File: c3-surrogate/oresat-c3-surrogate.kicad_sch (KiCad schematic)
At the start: 70 parts, among them J1 J-SAMTEC-TFM-120-X1-XXX-D-RA, J2 Conn_01x04, J4 Conn_01x02_Socket, Q1 PMV45EN, Q3 NTR2101P, Q4 NTR2101P, Q5 DMP3050LVT-7, SW2 Slide Switch, SW3 OS203011MV9QS1, SW4 EG1218, U1 MAX892LEUA+T, U2 LTC4412xS6, U4 LTC4412xS6, U5 TS5A21366, U6 Trinket-M0

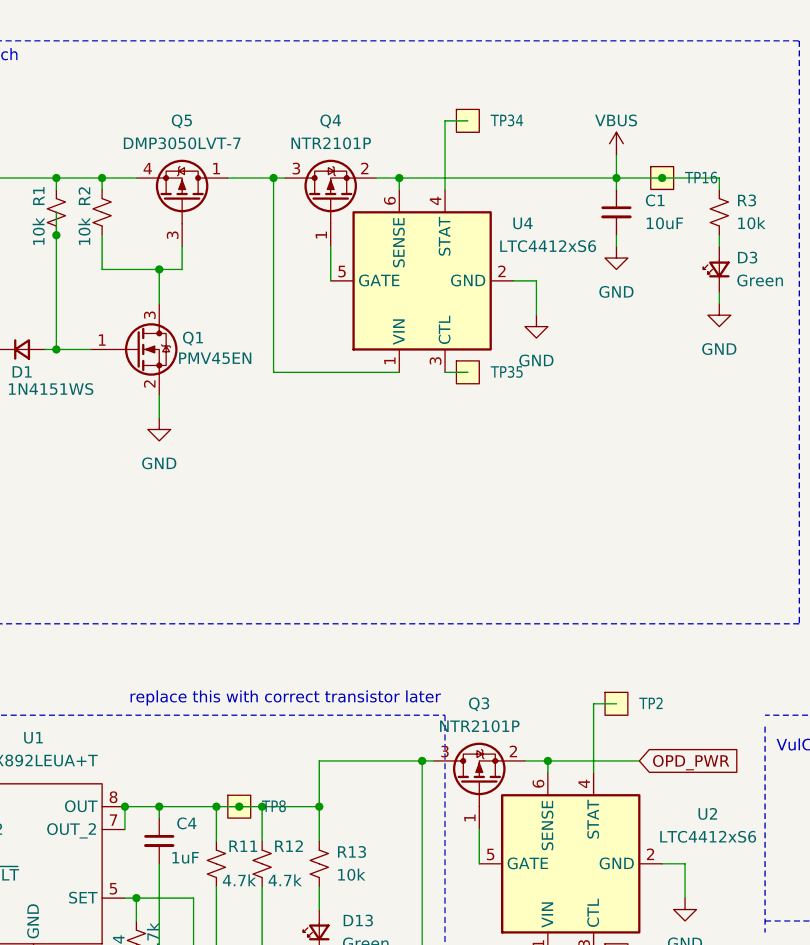
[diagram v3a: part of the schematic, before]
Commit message: modified pcb using updated schematic
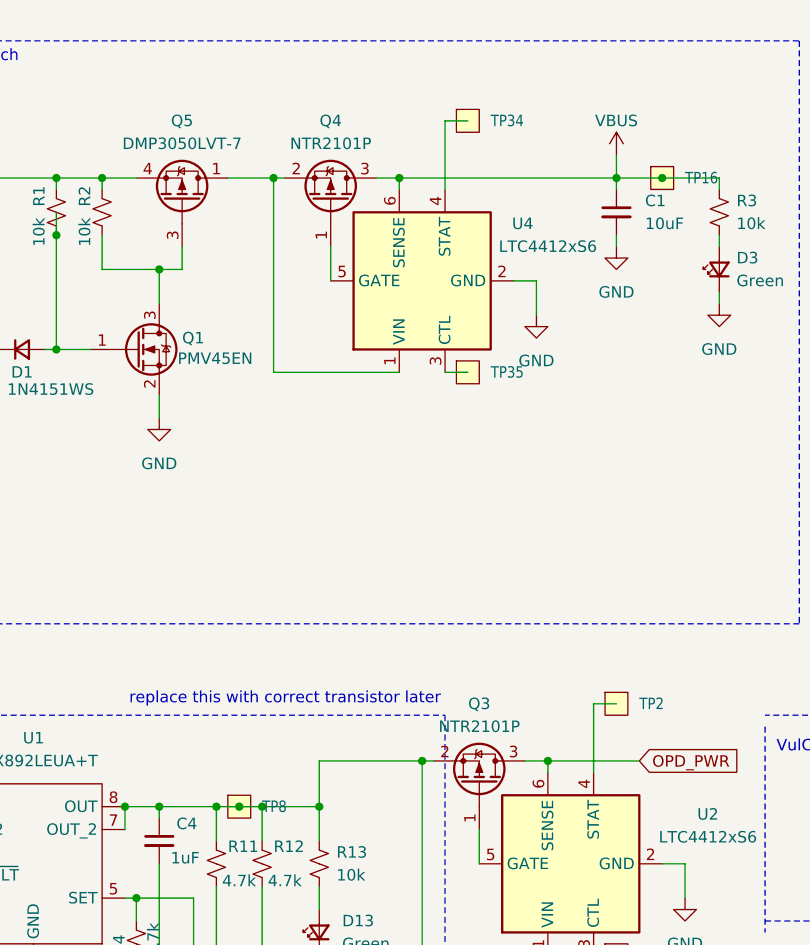
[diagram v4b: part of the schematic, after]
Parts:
- Q1: footprint Mosfets:SOT23-3 -> oresat-ics:SOT23
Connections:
- net OPD_PWR: now also Q3.3 (D); no longer Q3.2 (S)
- net VBUS: now also Q4.3 (D); no longer Q4.2 (S)
- net at Q5.1 (D), Q5.2 (D), Q5.5 (D)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: now also Q4.2 (S); no longer Q4.3 (D)
- net at C4.1, R11.1, R12.1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: now also Q3.2 (S); no longer Q3.3 (D)
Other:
- moved on the sheet: Q3, Q4
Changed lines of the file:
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@@
 	(symbol
 		(lib_id "Transistor_FET:NTR2101P")
-		(at 160.02 36.83 90)
+		(at 160.02 36.83 270)
+		(mirror x)
 		(unit 1)
 		(exclude_from_sim no)
@@
 		(on_board yes)
 		(dnp no)
-		(fields_autoplaced yes)
 		(property "Reference" "Q4"
 			(at 160.02 27.94 90)
@@
 		)
 		(property "Footprint" "Package_TO_SOT_SMD:SOT-23"
-			(at 161.925 31.75 0)
+			(at 158.115 31.75 0)
 			(effects
 				(font
@@
 		)
 		(property "Datasheet" "http://www.onsemi.com/pub/Collateral/NTR2101P-D.PDF"
-			(at 163.83 31.75 0)
+			(at 156.21 31.75 0)
 			(effects
 				(font
@@
 	(symbol
 		(lib_id "Transistor_FET:NTR2101P")
-		(at 176.53 101.6 90)
+		(at 176.53 101.6 270)
+		(mirror x)
 		(unit 1)
 		(exclude_from_sim no)
@@
 		(on_board yes)
 		(dnp no)
-		(fields_autoplaced yes)
 		(property "Reference" "Q3"
 			(at 176.53 92.71 90)
@@
 		)
 		(property "Footprint" "Package_TO_SOT_SMD:SOT-23"
-			(at 178.435 96.52 0)
+			(at 174.625 96.52 0)
 			(effects
 				(font
@@
 		)
 		(property "Datasheet" "http://www.onsemi.com/pub/Collateral/NTR2101P-D.PDF"
-			(at 180.34 96.52 0)
+			(at 172.72 96.52 0)
 			(effects
 				(font
@@
 			)
 		)
-		(property "Footprint" "Mosfets:SOT23-3"
+		(property "Footprint" "oresat-ics:SOT23"
 			(at 143.51 50.8 0)
 			(effects

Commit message: PCB edits
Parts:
- added TP20, TP36: Test-Point, oresat-misc:TestPoint-0.75mm-th, symbol oresat-misc:Test-Point-0.75mm-th
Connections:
- net C3-UART-RX: now also SW3.2; no longer SW3.4
- net C3-UART-TX: now also SW3.4; no longer SW3.2
- net CAN2_H: now also TP20.1
- net CAN2_L: now also TP36.1
- net at SW3.1: no longer R9.2
- net at SW3.5: now also R9.2
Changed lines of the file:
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@@
+	(symbol
+		(lib_id "oresat-misc:Test-Point-0.75mm-th")
+		(at 45.72 134.62 0)
+		(unit 1)
+		(exclude_from_sim yes)
+		(in_bom no)
+		(on_board yes)
+		(dnp no)
+		(fields_autoplaced yes)
+		(property "Reference" "TP20"
+			(at 48.26 134.6199 0)
+			(effects
+				(font
+					(size 1.27 1.0795)
+				)
+				(justify left)
+			)
+		)
+		(property "Value" "Test-Point"
+			(at 45.72 127 0)
+			(effects
+				(font
+					(size 1.27 1.27)
+				)
+				(hide yes)
+			)
+		)
+		(property "Footprint" "oresat-misc:TestPoint-0.75mm-th"
+			(at 45.72 124.46 0)
+			(effects
+				(font
+					(size 1.27 1.27)
+				)
+				(hide yes)
+			)
+		)
+		(property "Datasheet" ""
+			(at 45.72 134.62 0)
+			(effects
+				(font
+					(size 1.27 1.27)
+				)
+				(hide yes)
+			)
+		)
+		(property "Description" "0.75 mm TH test point; good for scope probes and jumpers"
+			(at 45.72 134.62 0)
+			(effects
+				(font
+					(size 1.27 1.27)
+				)
+				(hide yes)
+			)
+		)
+		(pin "1"
+		)
+		(instances
+			(project "oresat-c3-surrogate"
+				(path "/a762bfd7-2da3-46cd-8ea9-3793bee7a19f"
+					(reference "TP20")
+					(unit 1)
+				)
+			)
+		)
+	)
 	(symbol
 		(lib_id "oresat-misc:Test-Point-0.75mm-th")
@@
 					(unit 1)
 				)
+			)
+		)
+	)
+	(symbol
+		(lib_id "oresat-misc:Test-Point-0.75mm-th")
+		(at 45.72 137.16 0)
+		(unit 1)
+		(exclude_from_sim yes)
+		(in_bom no)
+		(on_board yes)
+		(dnp no)
+		(fields_autoplaced yes)
+		(property "Reference" "TP36"
+			(at 48.26 137.1599 0)
+			(effects
+				(font
+					(size 1.27 1.0795)
+				)
+				(justify left)
+			)
+		)
+		(property "Value" "Test-Point"
+			(at 45.72 129.54 0)
+			(effects
+				(font
+					(size 1.27 1.27)
+				)
+				(hide yes)
+			)
+		)
+		(property "Footprint" "oresat-misc:TestPoint-0.75mm-th"
+			(at 45.72 127 0)
+			(effects
+				(font
+					(size 1.27 1.27)
+				)
+				(hide yes)
+			)
+		)
+		(property "Datasheet" ""
+			(at 45.72 137.16 0)
+			(effects
+				(font
+					(size 1.27 1.27)
+				)
+				(hide yes)
+			)
+		)
+		(property "Description" "0.75 mm TH test point; good for scope probes and jumpers"
+			(at 45.72 137.16 0)
+			(effects
+				(font
+					(size 1.27 1.27)
+				)
+				(hide yes)
+			)
+		)
+		(pin "1"
+		)
+		(instances
+			(project "oresat-c3-surrogate"
+				(path "/a762bfd7-2da3-46cd-8ea9-3793bee7a19f"
+					(reference "TP36")
+					(unit 1)
+				)

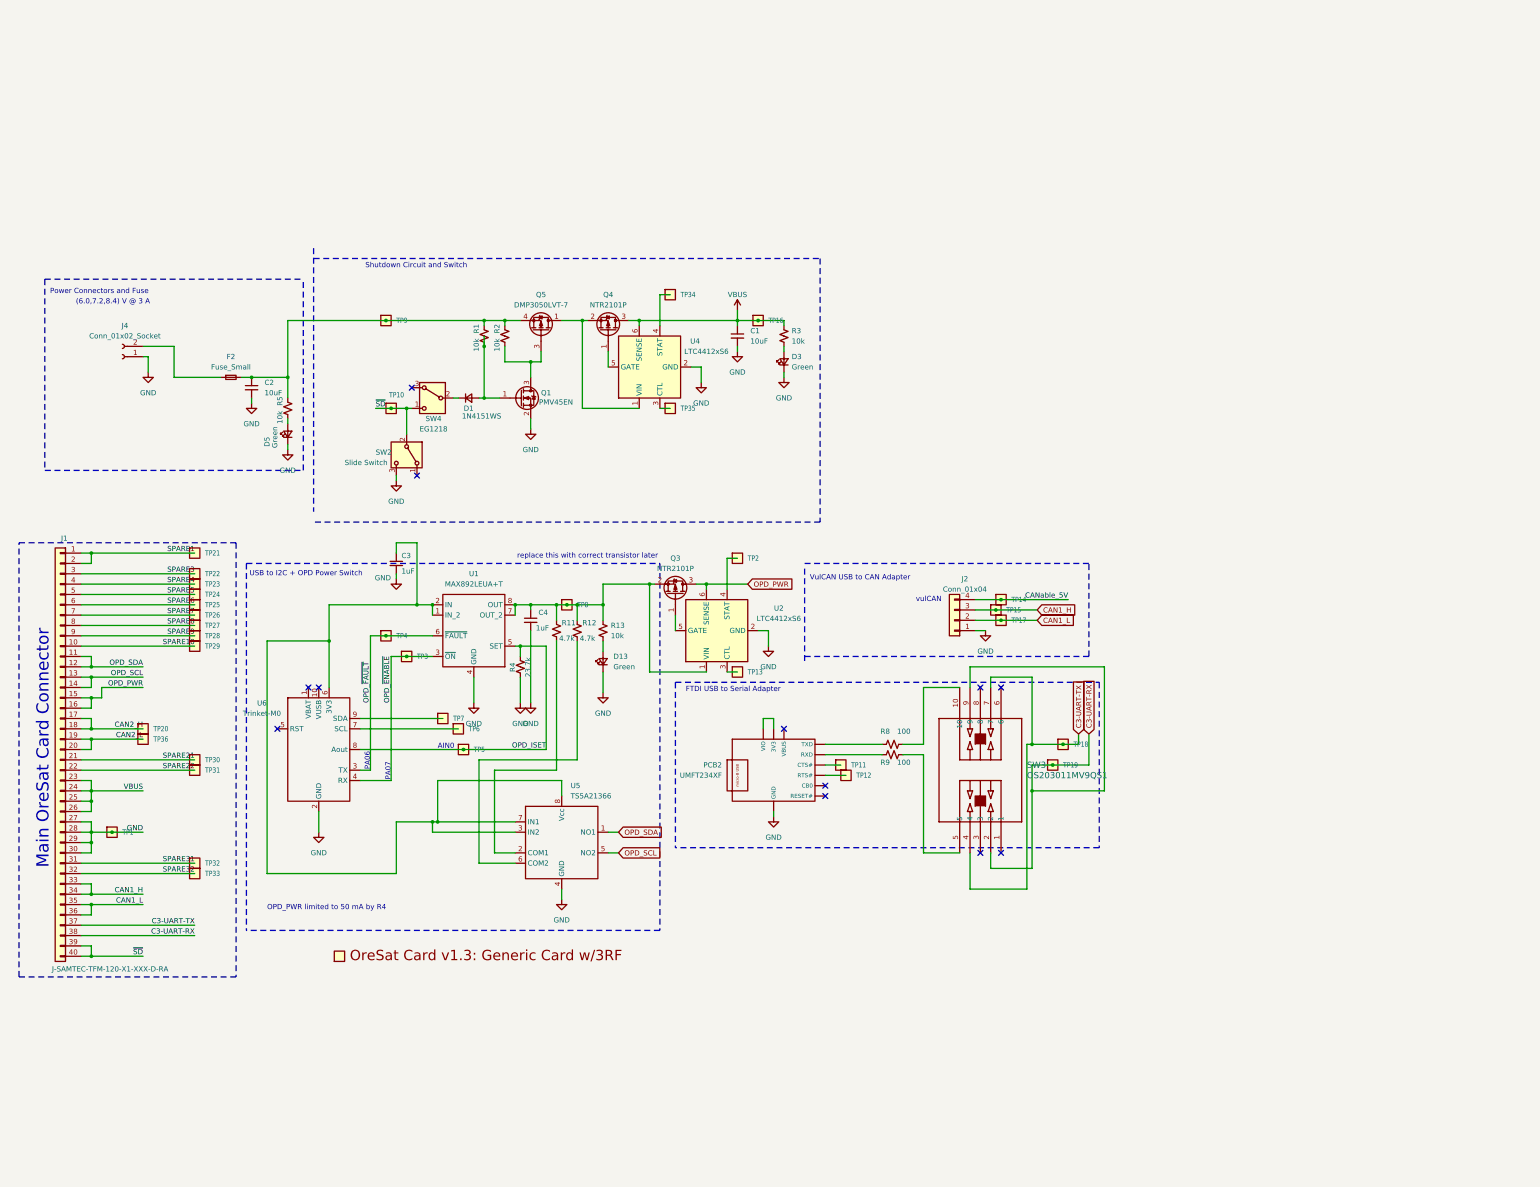
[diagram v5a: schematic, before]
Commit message: Found one schematic error (no I2C connections), and lots of stupid unecessary polishing because OCD. Also updated symbol and library footprints.
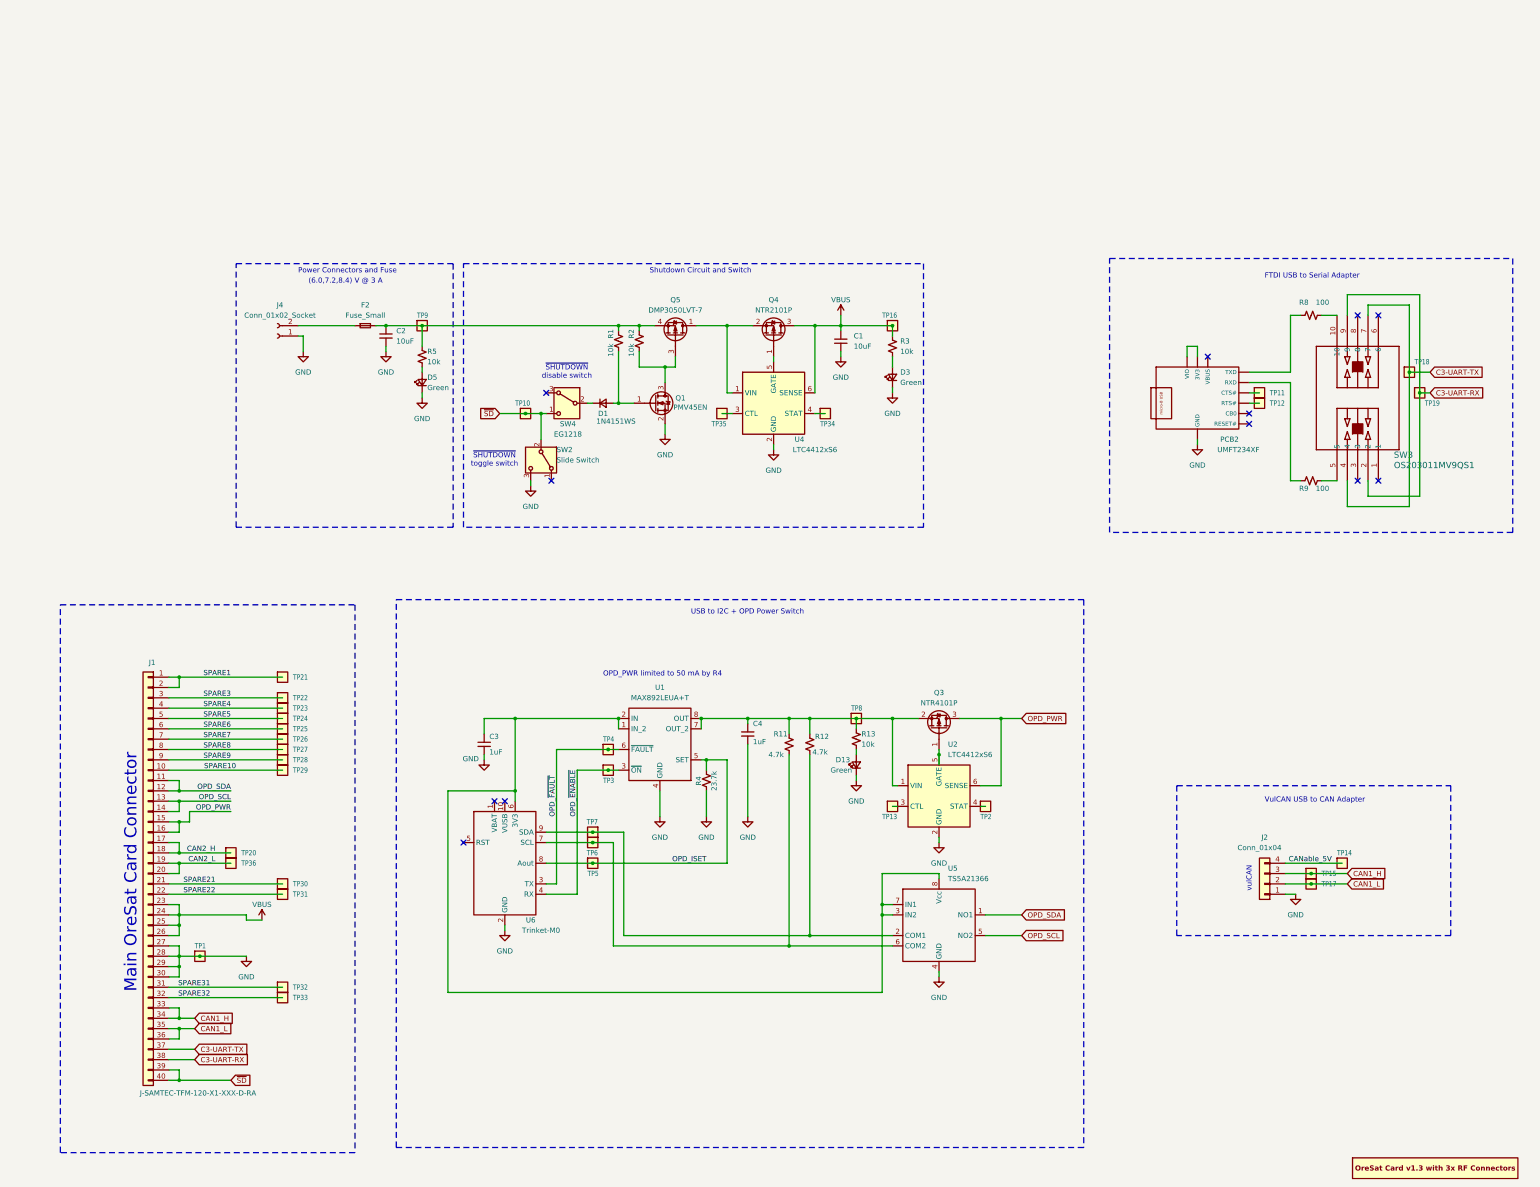
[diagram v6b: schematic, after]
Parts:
- J1: footprint J-SAMTEC-TFM-120-X1-XXX-D-RA:J-SAMTEC-TFM-120-X1-XXX-D-RA -> oresat-connectors:J-SAMTEC-TFM-120-X1-XXX-D-RA
- PCB1: footprint oresat-cards:ORESAT-CARD-V1.3-GENERIC-3RF -> oresat-pcbs:ORESAT-CARD-V1.3-3RF; symbol oresat-cards:ORESAT-CARD-V1.3-GENERIC-3RF -> oresat-pcbs:ORESAT-CARD-V1.3-3RF; now in the parts list
- Q3: value NTR2101P -> NTR4101P
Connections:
- net at R11.2: now also TP6.1, U5.6 (COM2), U6.7 (SCL); no longer U5.2 (COM1)
- net at TP7.1, U6.9 (SDA): now also R12.2, U5.2 (COM1)
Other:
- note added: "~{SHUTDOWN} disable switch"
- note added: "~{SHUTDOWN} toggle switch"
- note removed: "AIN0"
- note removed: "PA06"
- note removed: "PA07"
- note removed: "replace this with correct transistor later"
- title: (none) -> C3 Surrogate Card
- moved on the sheet: C1, C2, C3, C4, D1, D13, D3, D5, F2, J1, J2, J4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
